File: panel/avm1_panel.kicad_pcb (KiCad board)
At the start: 2 copper layers, 40.3 x 128.5 mm, 13 parts, among them J1 DNP

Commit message: Update panel for v1.1 gerbers
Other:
- board text added: "PANEL"

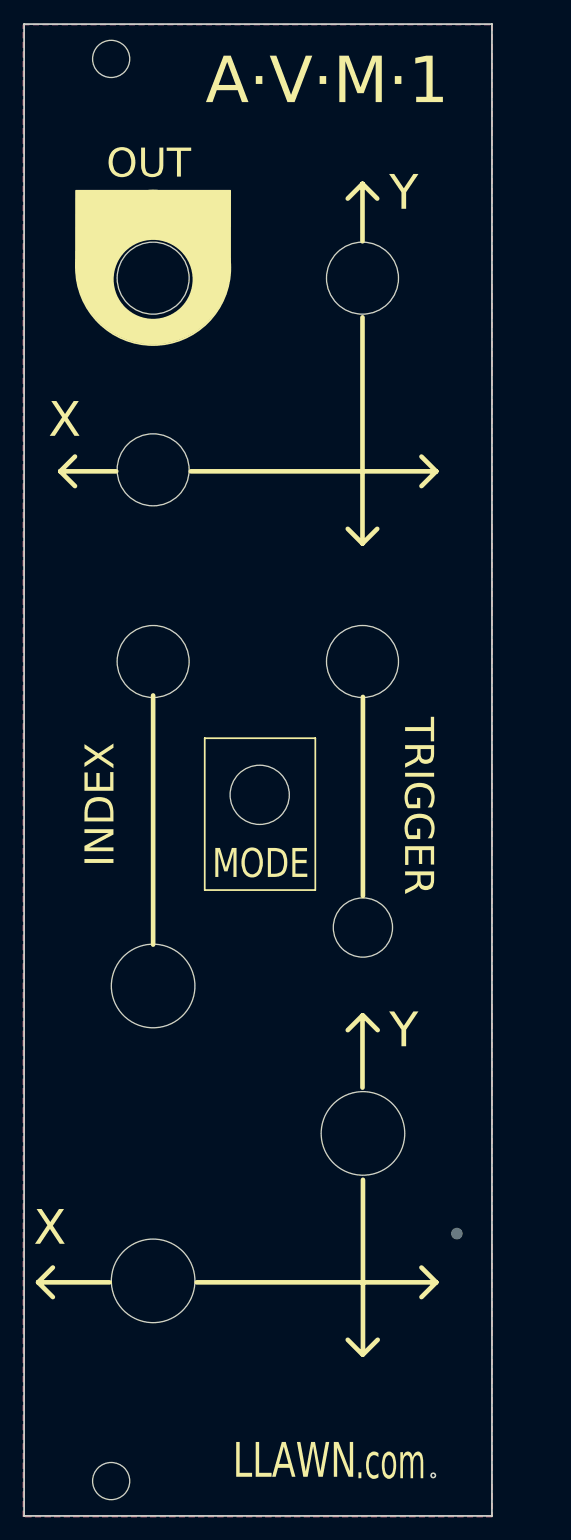
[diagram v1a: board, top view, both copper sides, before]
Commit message: Update panel with new logo and minor design change
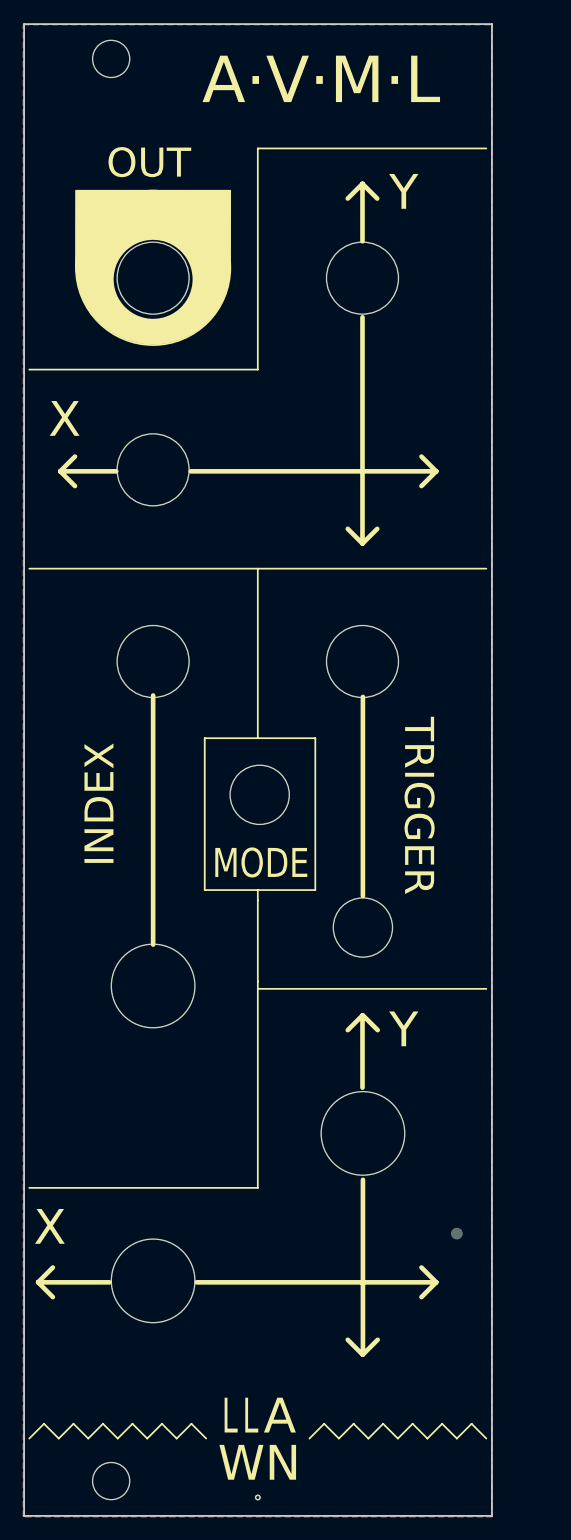
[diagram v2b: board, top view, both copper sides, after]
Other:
- board text added: "A"
- board text added: "A·V·M·L"
- board text added: "L"
- board text added: "WN"
- board text added: "v1.2 — 2022-10-20"
- board text removed: ".com"
- board text removed: "A·V·M·1"
- board text removed: "LLAWN"
- board text removed: "v1.1 — 2021-11-11"
